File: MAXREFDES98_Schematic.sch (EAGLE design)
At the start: 32 parts, among them U1 MB110S-TP, U2 MB110S-TP, U3 MAX5969AETB+

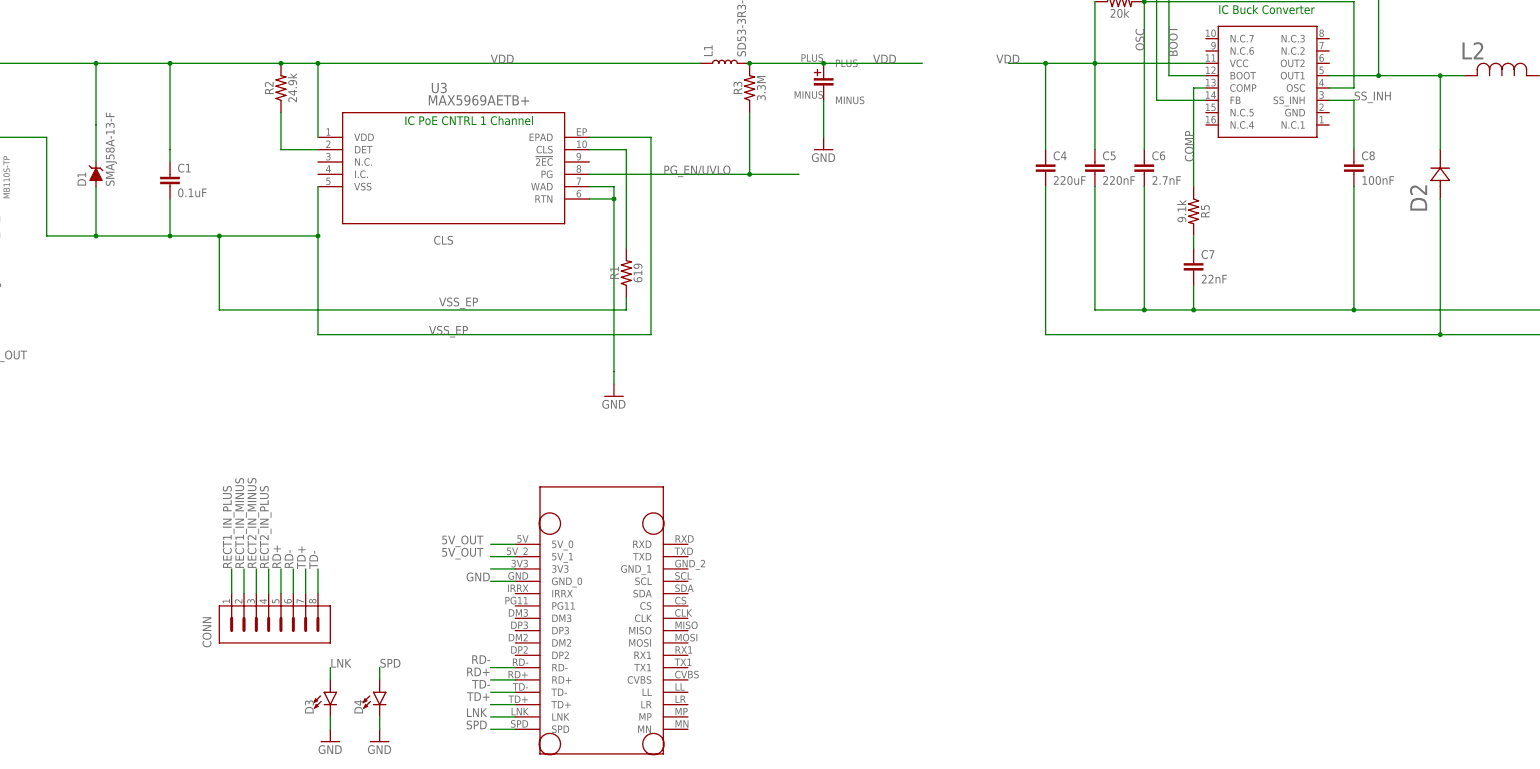
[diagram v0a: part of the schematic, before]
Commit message: Conneted PG_EN line to SS_INH and added limiting resistors for LEDs
Need to determine if SPD/LNK lines are active high or active low.
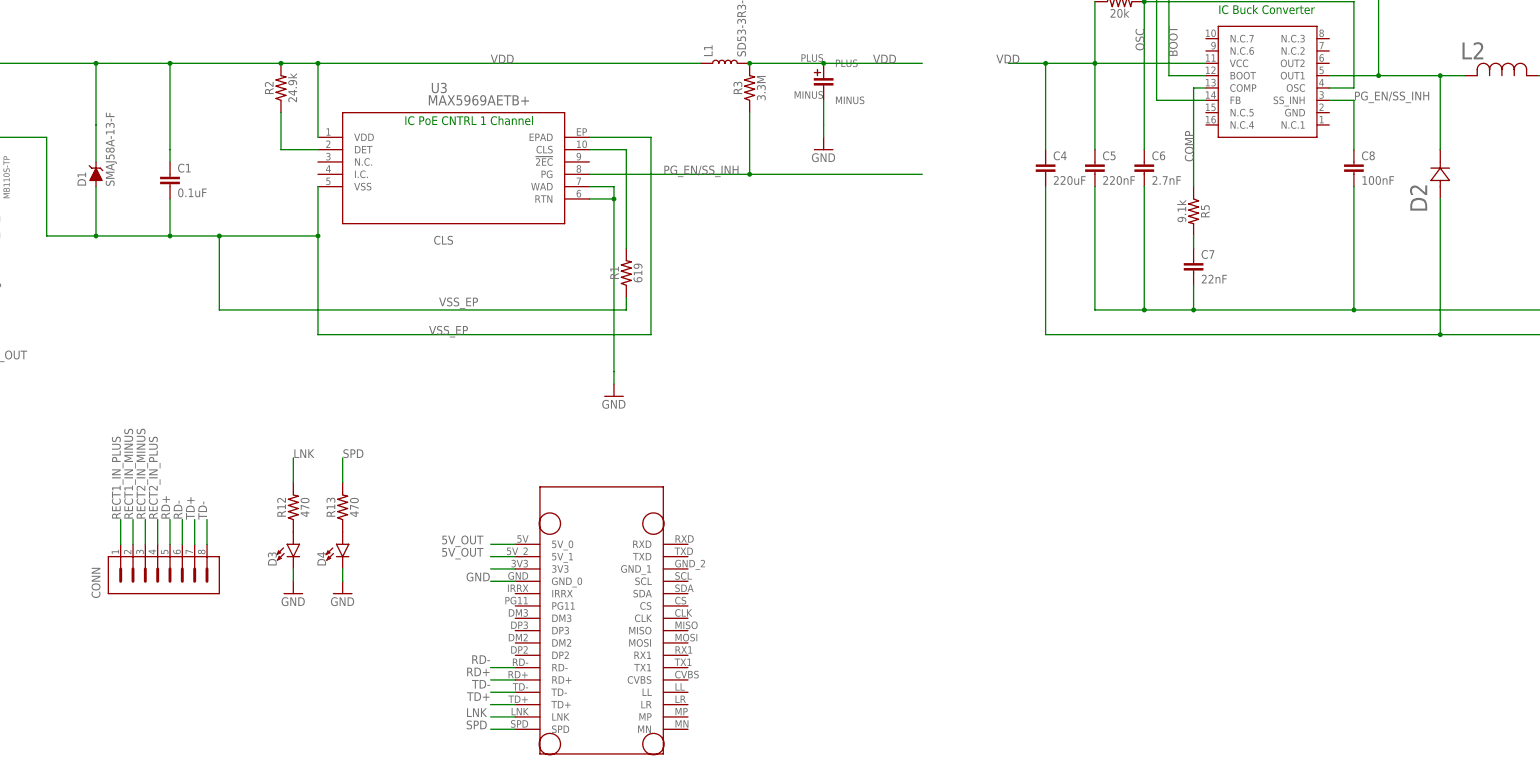
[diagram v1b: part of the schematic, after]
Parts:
- added R12, R13: 470, SparkFun-Resistors:0OHM-0603-1/10W-5%
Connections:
- removed net PG_EN/UVLO: R3.1, U3.PG
- removed net SS_INH: C8.1, U$1.SS_INH
- new net N$1: D3.A, R12.1
- new net N$2: D4.A, R13.1
- new net PG_EN/SS_INH: C8.1, R3.1, U$1.SS_INH, U3.PG
- net LNK: now also R12.2; no longer D3.A
- net SPD: now also R13.2; no longer D4.A
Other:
- moved on the sheet: CONN, D3, D4
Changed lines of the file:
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@@
 <part name="GND3" library="supply1" library_urn="urn:adsk.eagle:library:371" deviceset="GND" device=""/>
 <part name="GND4" library="supply1" library_urn="urn:adsk.eagle:library:371" deviceset="GND" device=""/>
+<part name="R12" library="SparkFun-Resistors" library_urn="urn:adsk.eagle:library:532" deviceset="0OHM" device="-0603-1/10W-5%" package3d_urn="urn:adsk.eagle:package:39650/1" value="470"/>
+<part name="R13" library="SparkFun-Resistors" library_urn="urn:adsk.eagle:library:532" deviceset="0OHM" device="-0603-1/10W-5%" package3d_urn="urn:adsk.eagle:package:39650/1" value="470"/>
 </parts>
 <sheets>
@@
 <attribute name="DRAWING_NAME" x="203.2" y="-125.73" size="2.54" layer="94"/>
 </instance>
-<instance part="CONN" gate="G$1" x="-45.72" y="-88.9" smashed="yes">
-<attribute name="NAME" x="-47.371" y="-97.536" size="1.778" layer="95" rot="R90"/>
+<instance part="CONN" gate="G$1" x="-68.58" y="-78.74" smashed="yes">
+<attribute name="NAME" x="-70.231" y="-87.376" size="1.778" layer="95" rot="R90"/>
 </instance>
 <instance part="U$2" gate="G$1" x="20.32" y="-119.38" smashed="yes"/>
@@
 <attribute name="VALUE" x="241.3" y="-38.1" size="1.778" layer="96"/>
 </instance>
-<instance part="D3" gate="G$1" x="-22.86" y="-106.68" smashed="yes">
-<attribute name="NAME" x="-26.289" y="-111.252" size="1.778" layer="95" font="vector" rot="R90"/>
-<attribute name="VALUE" x="-20.955" y="-111.252" size="1.778" layer="96" font="vector" rot="R90" align="top-left"/>
-</instance>
-<instance part="D4" gate="G$1" x="-12.7" y="-106.68" smashed="yes">
-<attribute name="NAME" x="-16.129" y="-111.252" size="1.778" layer="95" font="vector" rot="R90"/>
-<attribute name="VALUE" x="-10.795" y="-111.252" size="1.778" layer="96" font="vector" rot="R90" align="top-left"/>
-</instance>
-<instance part="GND3" gate="1" x="-22.86" y="-116.84" smashed="yes">
-<attribute name="VALUE" x="-25.4" y="-119.38" size="1.778" layer="96"/>
-</instance>
-<instance part="GND4" gate="1" x="-12.7" y="-116.84" smashed="yes">
-<attribute name="VALUE" x="-15.24" y="-119.38" size="1.778" layer="96"/>
+<instance part="D3" gate="G$1" x="-30.48" y="-76.2" smashed="yes">
+<attribute name="NAME" x="-33.909" y="-80.772" size="1.778" layer="95" font="vector" rot="R90"/>
+<attribute name="VALUE" x="-28.575" y="-80.772" size="1.778" layer="96" font="vector" rot="R90" align="top-left"/>
+</instance>
+<instance part="D4" gate="G$1" x="-20.32" y="-76.2" smashed="yes">
+<attribute name="NAME" x="-23.749" y="-80.772" size="1.778" layer="95" font="vector" rot="R90"/>
+<attribute name="VALUE" x="-18.415" y="-80.772" size="1.778" layer="96" font="vector" rot="R90" align="top-left"/>
+</instance>
+<instance part="GND3" gate="1" x="-30.48" y="-86.36" smashed="yes">
+<attribute name="VALUE" x="-33.02" y="-88.9" size="1.778" layer="96"/>
+</instance>
+<instance part="GND4" gate="1" x="-20.32" y="-86.36" smashed="yes">
+<attribute name="VALUE" x="-22.86" y="-88.9" size="1.778" layer="96"/>
+</instance>
+<instance part="R12" gate="G$1" x="-30.48" y="-68.58" smashed="yes" rot="R90">
+<attribute name="NAME" x="-32.004" y="-68.58" size="1.778" layer="95" font="vector" rot="R90" align="bottom-center"/>
+<attribute name="VALUE" x="-28.956" y="-68.58" size="1.778" layer="96" font="vector" rot="R90" align="top-center"/>
+</instance>
+<instance part="R13" gate="G$1" x="-20.32" y="-68.58" smashed="yes" rot="R90">
+<attribute name="NAME" x="-21.844" y="-68.58" size="1.778" layer="95" font="vector" rot="R90" align="bottom-center"/>
+<attribute name="VALUE" x="-18.796" y="-68.58" size="1.778" layer="96" font="vector" rot="R90" align="top-center"/>
 </instance>
 </instances>
@@
 </segment>
 </net>
-<net name="PG_EN/UVLO" class="0">
+<net name="PG_EN/SS_INH" class="0">
 <segment>
 <pinref part="U3" gate="G$1" pin="PG"/>
@@
 <wire x1="63.5" y1="0" x2="63.5" y2="12.7" width="0.1524" layer="91"/>
 <label x="45.72" y="0" size="1.778" layer="95"/>
-<wire x1="63.5" y1="0" x2="73.66" y2="0" width="0.1524" layer="91"/>
 <junction x="63.5" y="0"/>
+<wire x1="63.5" y1="0" x2="99.06" y2="0" width="0.1524" layer="91"/>
+</segment>
+<segment>
+<pinref part="U$1" gate="G$1" pin="SS_INH"/>
+<wire x1="182.88" y1="15.24" x2="187.96" y2="15.24" width="0.1524" layer="91"/>
+<pinref part="C8" gate="G$1" pin="1"/>
+<wire x1="187.96" y1="15.24" x2="187.96" y2="5.08" width="0.1524" layer="91"/>
+<label x="187.96" y="15.24" size="1.778" layer="95"/>
 </segment>
 </net>
@@
 <segment>
 <pinref part="D3" gate="G$1" pin="C"/>
-<wire x1="-22.86" y1="-111.76" x2="-22.86" y2="-114.3" width="0.1524" layer="91"/>
+<wire x1="-30.48" y1="-81.28" x2="-30.48" y2="-83.82" width="0.1524" layer="91"/>
 <pinref part="GND3" gate="1" pin="GND"/>
 </segment>
 <segment>
 <pinref part="D4" gate="G$1" pin="C"/>
-<wire x1="-12.7" y1="-111.76" x2="-12.7" y2="-114.3" width="0.1524" layer="91"/>
+<wire x1="-20.32" y1="-81.28" x2="-20.32" y2="-83.82" width="0.1524" layer="91"/>
 <pinref part="GND4" gate="1" pin="GND"/>
 </segment>
@@
 <net name="RD+" class="0">
 <segment>
-<wire x1="-33.02" y1="-86.36" x2="-33.02" y2="-81.28" width="0.1524" layer="91"/>
+<wire x1="-55.88" y1="-76.2" x2="-55.88" y2="-71.12" width="0.1524" layer="91"/>
 <pinref part="CONN" gate="G$1" pin="5"/>
-<label x="-33.02" y="-81.28" size="1.778" layer="95" rot="R90"/>
+<label x="-55.88" y="-71.12" size="1.778" layer="95" rot="R90"/>
 </segment>
 <segment>
@@
 <segment>
 <pinref part="CONN" gate="G$1" pin="2"/>
-<wire x1="-40.64" y1="-86.36" x2="-40.64" y2="-81.28" width="0.1524" layer="91"/>
-<label x="-40.64" y="-81.28" size="1.778" layer="95" rot="R90"/>
+<wire x1="-63.5" y1="-76.2" x2="-63.5" y2="-71.12" width="0.1524" layer="91"/>
+<label x="-63.5" y="-71.12" size="1.778" layer="95" rot="R90"/>
 </segment>
 <segment>
@@
 <segment>
 <pinref part="CONN" gate="G$1" pin="1"/>
-<wire x1="-43.18" y1="-86.36" x2="-43.18" y2="-81.28" width="0.1524" layer="91"/>
-<label x="-43.18" y="-81.28" size="1.778" layer="95" rot="R90"/>
+<wire x1="-66.04" y1="-76.2" x2="-66.04" y2="-71.12" width="0.1524" layer="91"/>
+<label x="-66.04" y="-71.12" size="1.778" layer="95" rot="R90"/>
 </segment>
 <segment>
@@
 <segment>
 <pinref part="CONN" gate="G$1" pin="3"/>
-<wire x1="-38.1" y1="-86.36" x2="-38.1" y2="-81.28" width="0.1524" layer="91"/>
-<label x="-38.1" y="-81.28" size="1.778" layer="95" rot="R90"/>
+<wire x1="-60.96" y1="-76.2" x2="-60.96" y2="-71.12" width="0.1524" layer="91"/>
+<label x="-60.96" y="-71.12" size="1.778" layer="95" rot="R90"/>
 </segment>
 <segment>
@@
 <segment>
 <pinref part="CONN" gate="G$1" pin="4"/>
-<wire x1="-35.56" y1="-86.36" x2="-35.56" y2="-81.28" width="0.1524" layer="91"/>
-<label x="-35.56" y="-81.28" size="1.778" layer="95" rot="R90"/>
+<wire x1="-58.42" y1="-76.2" x2="-58.42" y2="-71.12" width="0.1524" layer="91"/>
+<label x="-58.42" y="-71.12" size="1.778" layer="95" rot="R90"/>
 </segment>
 <segment>
@@
 <segment>
 <pinref part="CONN" gate="G$1" pin="6"/>
-<wire x1="-30.48" y1="-86.36" x2="-30.48" y2="-81.28" width="0.1524" layer="91"/>
-<label x="-30.48" y="-81.28" size="1.778" layer="95" rot="R90"/>
+<wire x1="-53.34" y1="-76.2" x2="-53.34" y2="-71.12" width="0.1524" layer="91"/>
+<label x="-53.34" y="-71.12" size="1.778" layer="95" rot="R90"/>
 </segment>
 <segment>
@@
 <segment>
 <pinref part="CONN" gate="G$1" pin="7"/>
-<wire x1="-27.94" y1="-86.36" x2="-27.94" y2="-81.28" width="0.1524" layer="91"/>
-<label x="-27.94" y="-81.28" size="1.778" layer="95" rot="R90"/>
+<wire x1="-50.8" y1="-76.2" x2="-50.8" y2="-71.12" width="0.1524" layer="91"/>
+<label x="-50.8" y="-71.12" size="1.778" layer="95" rot="R90"/>
 </segment>
 <segment>
@@
 <segment>
 <pinref part="CONN" gate="G$1" pin="8"/>
-<wire x1="-25.4" y1="-86.36" x2="-25.4" y2="-81.28" width="0.1524" layer="91"/>
-<label x="-25.4" y="-81.28" size="1.778" layer="95" rot="R90"/>
+<wire x1="-48.26" y1="-76.2" x2="-48.26" y2="-71.12" width="0.1524" layer="91"/>
+<label x="-48.26" y="-71.12" size="1.778" layer="95" rot="R90"/>
 </segment>
 <segment>
@@
 <wire x1="154.94" y1="17.78" x2="157.48" y2="17.78" width="0.1524" layer="91"/>
 <label x="154.94" y="2.54" size="1.778" layer="95" rot="R90"/>
-</segment>
-</net>
-<net name="SS_INH" class="0">
-<segment>
-<pinref part="U$1" gate="G$1" pin="SS_INH"/>
-<wire x1="182.88" y1="15.24" x2="187.96" y2="15.24" width="0.1524" layer="91"/>
-<pinref part="C8" gate="G$1" pin="1"/>
-<wire x1="187.96" y1="15.24" x2="187.96" y2="5.08" width="0.1524" layer="91"/>
-<label x="187.96" y="15.24" size="1.778" layer="95"/>
 </segment>
 </net>
@@
 </segment>
 <segment>
-<pinref part="D3" gate="G$1" pin="A"/>
-<wire x1="-22.86" y1="-104.14" x2="-22.86" y2="-101.6" width="0.1524" layer="91"/>
-<label x="-22.86" y="-101.6" size="1.778" layer="95"/>
+<pinref part="R12" gate="G$1" pin="2"/>
+<wire x1="-30.48" y1="-63.5" x2="-30.48" y2="-58.42" width="0.1524" layer="91"/>
+<label x="-30.48" y="-58.42" size="1.778" layer="95"/>
 </segment>
 </net>
@@
 </segment>
 <segment>
+<pinref part="R13" gate="G$1" pin="2"/>
+<wire x1="-20.32" y1="-63.5" x2="-20.32" y2="-58.42" width="0.1524" layer="91"/>
+<label x="-20.32" y="-58.42" size="1.778" layer="95"/>
+</segment>
+</net>
+<net name="N$1" class="0">
+<segment>
+<pinref part="R12" gate="G$1" pin="1"/>
+<pinref part="D3" gate="G$1" pin="A"/>
+</segment>
+</net>
+<net name="N$2" class="0">
+<segment>
+<pinref part="R13" gate="G$1" pin="1"/>
 <pinref part="D4" gate="G$1" pin="A"/>
-<wire x1="-12.7" y1="-104.14" x2="-12.7" y2="-101.6" width="0.1524" layer="91"/>
-<label x="-12.7" y="-101.6" size="1.778" layer="95"/>
-</segment>
-</net>
+</segment>
+</net>

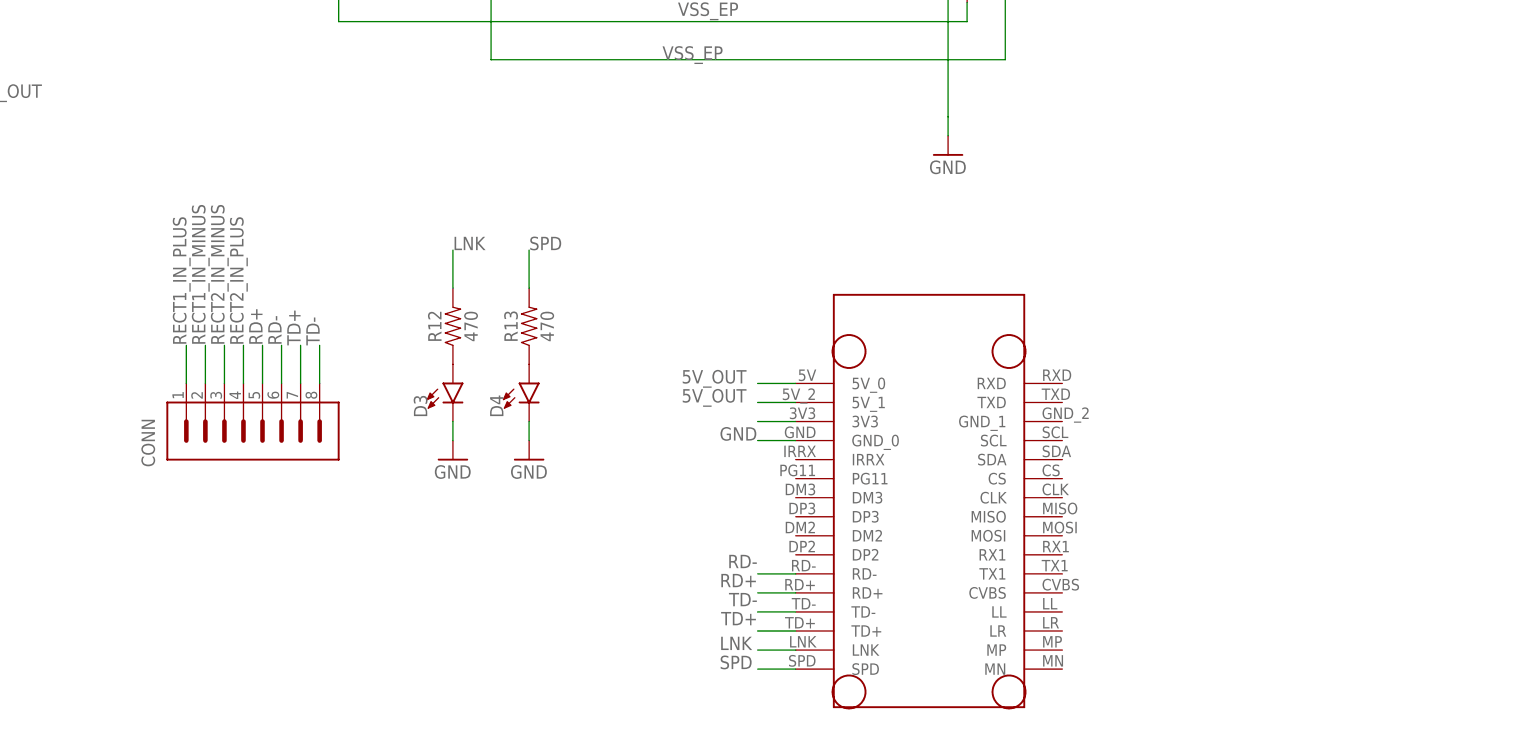
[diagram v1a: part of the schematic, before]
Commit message: Worked on schematic/checking component values
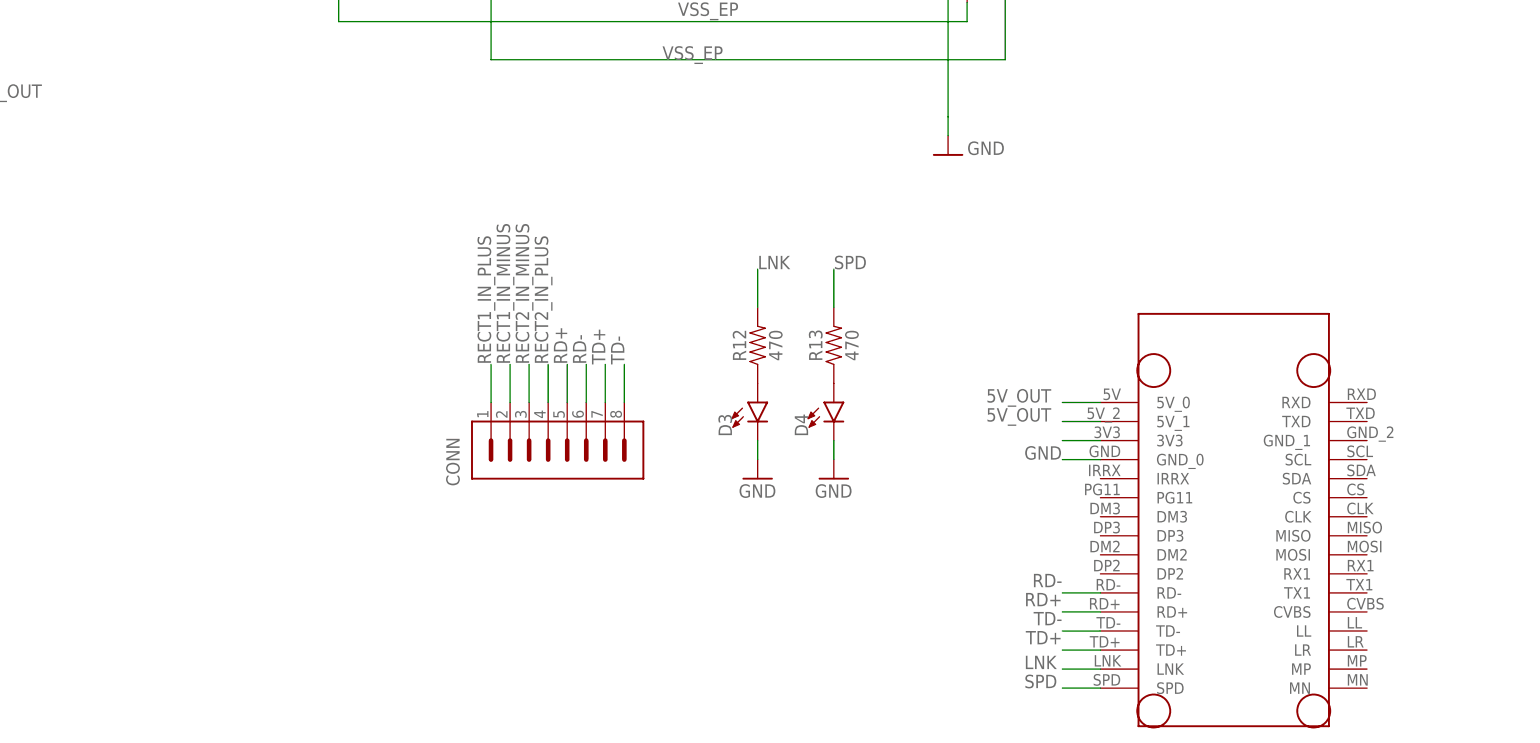
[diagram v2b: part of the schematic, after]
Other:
- moved on the sheet: CONN, D3, D4, R12, R13
